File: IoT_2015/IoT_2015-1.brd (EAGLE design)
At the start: 30 x 20 mm, 28 parts, among them Y1 ABLS-16.000MHZ-B4-T

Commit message: FITT EAGLE
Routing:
- net GND: track 144.9 -> 91.2 mm, vias 4 -> 2
- net N$27: track 0.00 -> 2.60 mm
- net N$21: track 0.00 -> 2.55 mm
- net VDD: track 103.9 -> 106.3 mm
- net N$28: track 0.00 -> 2.35 mm
- net N$42: track 0.00 -> 1.95 mm
- net N$44: track 0.00 -> 1.83 mm
- net N$32: track 0.00 -> 1.75 mm
- net N$29: track 0.00 -> 1.55 mm
- net N$19: track 0.00 -> 1.50 mm
- net N$43: track 0.00 -> 1.23 mm
- net N$40: track 0.00 -> 0.85 mm
- net N$38: track 0.00 -> 0.65 mm
- net N$37: track 0.00 -> 0.65 mm
- net N$14: track 0.00 -> 0.60 mm
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
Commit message: Test av jordlager
titta på dennna?
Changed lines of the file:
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@@
 <?xml version="1.0" encoding="utf-8"?>
 <!DOCTYPE eagle SYSTEM "eagle.dtd">
-<eagle version="7.3.0">
+<eagle version="7.2.0">
 <drawing>
 <settings>
@@
 <wire x1="13.96" y1="10.68" x2="16.4" y2="10.68" width="0.254" layer="1"/>
 <wire x1="16.4" y1="10.68" x2="16.4" y2="11.08" width="0.254" layer="1"/>
+<polygon width="0.01" layer="1" spacing="0.05" isolate="0.012">
+<vertex x="0" y="0"/>
+<vertex x="0" y="20"/>
+<vertex x="30" y="20"/>
+<vertex x="30" y="0"/>
+</polygon>
+<wire x1="16.21" y1="15.13" x2="13.35" y2="15.18" width="0" layer="19" extent="1-1"/>
+<wire x1="20.07" y1="12.25" x2="19.49" y2="15.13" width="0" layer="19" extent="1-1"/>
+<wire x1="8.92" y1="15.18" x2="13.2588" y2="15.3162" width="0" layer="19" extent="1-1"/>
 </signal>
 <signal name="N$3">

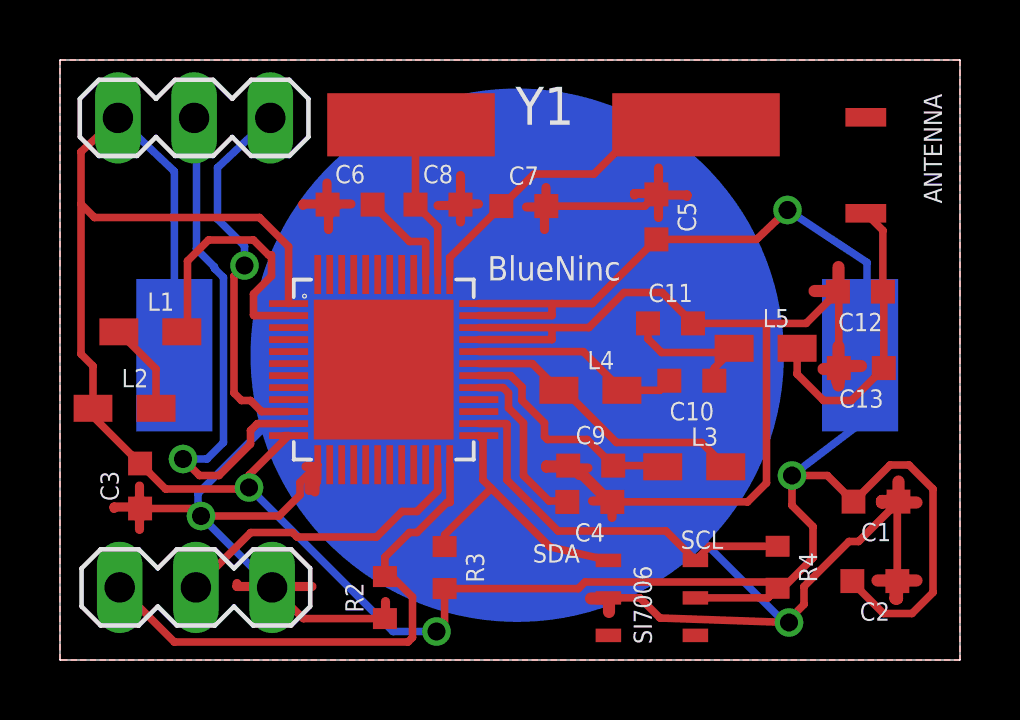
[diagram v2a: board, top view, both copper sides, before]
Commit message: groundplane
groundplane for top and bottom layer are done. To adjust the width of
the copper pour: Set the width of the polygon to draw around the design.
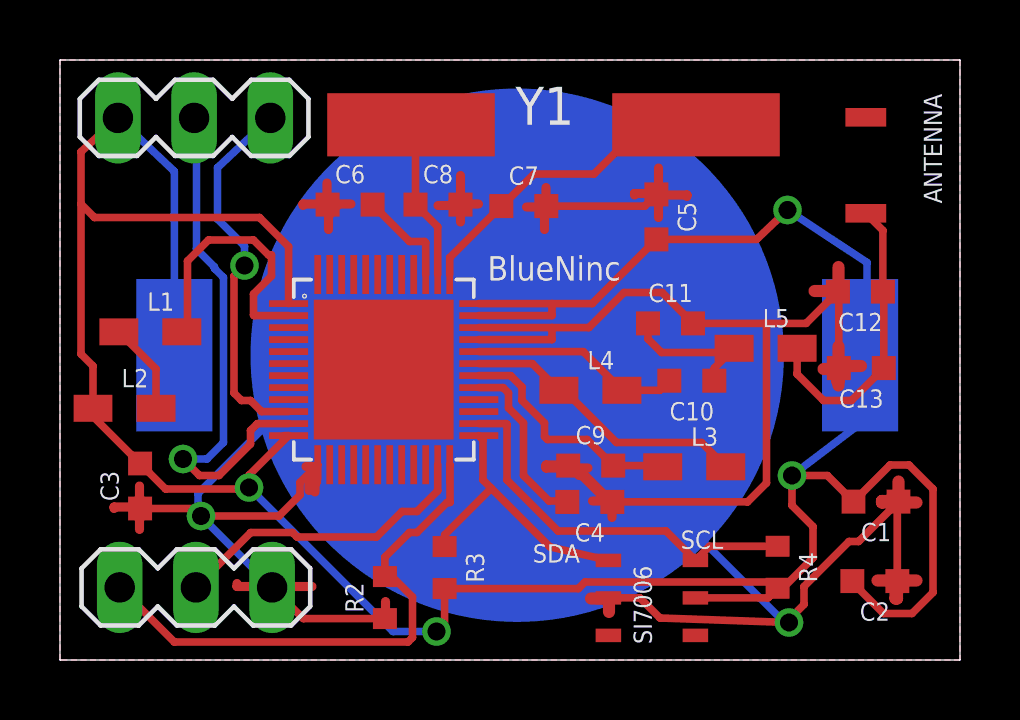
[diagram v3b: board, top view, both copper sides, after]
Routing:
- added copper zone on layer 1, net N$45
- added copper zone on layer 16, net N$46
- removed copper zone on layer 1, net GND

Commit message: Uploaded gerber files
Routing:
- net GND: track 91.2 -> 150.8 mm, vias 2 -> 5
- net N$21: track 2.55 -> 0.00 mm
- net N$28: track 2.35 -> 0.00 mm
- net N$42: track 1.95 -> 0.00 mm
- net N$32: track 1.75 -> 0.00 mm
- net N$29: track 1.55 -> 0.00 mm
- net N$19: track 1.50 -> 0.00 mm
- net N$43: track 1.23 -> 0.00 mm
- net N$40: track 0.85 -> 0.00 mm
- net N$38: track 0.65 -> 0.00 mm
- net N$37: track 0.65 -> 0.00 mm
- net N$14: track 0.60 -> 0.00 mm
- net N$25: track 0.60 -> 0.00 mm
- net N$36: track 0.55 -> 0.00 mm
- net N$30: track 0.55 -> 0.00 mm
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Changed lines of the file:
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@@
 <?xml version="1.0" encoding="utf-8"?>
 <!DOCTYPE eagle SYSTEM "eagle.dtd">
-<eagle version="7.2.0">
+<eagle version="7.3.0">
 <drawing>
 <settings>
@@
 <contactref element="SI7006" pad="GND"/>
 <contactref element="JTAG" pad="3"/>
-<wire x1="13.2588" y1="15.3162" x2="13.35" y2="15.18" width="0.254" layer="1"/>
 <wire x1="27.91" y1="2.63" x2="27.91" y2="5.24" width="0.254" layer="1"/>
 <wire x1="27.91" y1="5.24" x2="27.95" y2="5.28" width="0.254" layer="1"/>
-<wire x1="25.96" y1="9.73" x2="25.96" y2="12.25" width="0.254" layer="1"/>
-<wire x1="25.96" y1="12.25" x2="25.93" y2="12.28" width="0.254" layer="1"/>
 <wire x1="18.28" y1="2.07" x2="19.33" y2="2.07" width="0.254" layer="1"/>
 <wire x1="19.33" y1="2.07" x2="20" y2="1.4" width="0.254" layer="1"/>
@@
 <wire x1="26.3" y1="3.95" x2="26.62" y2="3.95" width="0.254" layer="1"/>
 <wire x1="26.62" y1="3.95" x2="27.95" y2="5.28" width="0.254" layer="1"/>
-<wire x1="16.94" y1="6.48" x2="17.2" y2="6.48" width="0.254" layer="1"/>
-<wire x1="17.2" y1="6.48" x2="18.41" y2="5.27" width="0.254" layer="1"/>
 <wire x1="21.1" y1="11.22" x2="23.5" y2="11.22" width="0.254" layer="1"/>
 <wire x1="23.5" y1="11.22" x2="24.87" y2="11.22" width="0.254" layer="1"/>
@@
 <wire x1="13.96" y1="10.68" x2="16.4" y2="10.68" width="0.254" layer="1"/>
 <wire x1="16.4" y1="10.68" x2="16.4" y2="11.08" width="0.254" layer="1"/>
-<wire x1="13.35" y1="15.18" x2="16.21" y2="15.13" width="0" layer="19" extent="1-1"/>
-<wire x1="20.07" y1="12.25" x2="19.49" y2="15.13" width="0" layer="19" extent="1-1"/>
-<wire x1="15.24" y1="10.16" x2="16.4" y2="10.68" width="0" layer="19" extent="1-16"/>
-<wire x1="8.92" y1="15.18" x2="13.2588" y2="15.3162" width="0" layer="19" extent="1-1"/>
+<wire x1="16.94" y1="6.48" x2="17.2" y2="6.48" width="0.254" layer="1"/>
+<wire x1="17.2" y1="6.48" x2="18.41" y2="5.27" width="0.254" layer="1"/>
+<wire x1="25.96" y1="9.73" x2="25.96" y2="12.25" width="0.254" layer="1"/>
+<wire x1="25.96" y1="12.25" x2="25.93" y2="12.28" width="0.254" layer="1"/>
+<wire x1="19.49" y1="15.13" x2="23.13" y2="15.13" width="0.254" layer="1"/>
+<wire x1="23.13" y1="15.13" x2="24.3" y2="16.3" width="0.254" layer="1"/>
+<wire x1="24.3" y1="16.3" x2="25" y2="16.3" width="0.254" layer="1"/>
+<via x="25" y="16.3" extent="1-16" drill="0.6"/>
+<wire x1="25" y1="16.3" x2="21.38" y2="16.3" width="0.254" layer="16"/>
+<wire x1="21.38" y1="16.3" x2="15.24" y2="10.16" width="0.254" layer="16"/>
+<wire x1="13.35" y1="15.18" x2="13.35" y2="15.25" width="0.254" layer="1"/>
+<wire x1="13.35" y1="15.25" x2="14.3" y2="16.2" width="0.254" layer="1"/>
+<wire x1="14.3" y1="16.2" x2="14.75" y2="16.2" width="0.254" layer="1"/>
+<wire x1="14.75" y1="16.2" x2="17.95" y2="19.4" width="0.254" layer="1"/>
+<wire x1="17.95" y1="19.4" x2="24.25" y2="19.4" width="0.254" layer="1"/>
+<wire x1="24.25" y1="19.4" x2="25.05" y2="18.6" width="0.254" layer="1"/>
+<wire x1="25.05" y1="18.6" x2="25.05" y2="16.35" width="0.254" layer="1"/>
+<wire x1="25.05" y1="16.35" x2="25" y2="16.3" width="0.254" layer="1"/>
+<wire x1="8.92" y1="15.18" x2="7.37" y2="15.18" width="0.254" layer="1"/>
+<wire x1="7.37" y1="15.18" x2="6.85" y2="15.7" width="0.254" layer="1"/>
+<via x="6.85" y="15.7" extent="1-16" drill="0.6"/>
+<wire x1="6.85" y1="15.7" x2="9.7" y2="15.7" width="0.254" layer="16"/>
+<wire x1="9.7" y1="15.7" x2="15.24" y2="10.16" width="0.254" layer="16"/>
+<wire x1="15.24" y1="10.16" x2="21.46" y2="10.16" width="0.254" layer="16"/>
+<wire x1="21.46" y1="10.16" x2="24.55" y2="13.25" width="0.254" layer="16"/>
+<via x="24.55" y="13.25" extent="1-16" drill="0.6"/>
+<wire x1="24.55" y1="13.25" x2="24.96" y2="13.25" width="0.254" layer="1"/>
+<wire x1="24.96" y1="13.25" x2="25.93" y2="12.28" width="0.254" layer="1"/>
 </signal>
 <signal name="N$3">
@@
 </signal>
 <signal name="N$13">
-<wire x1="25.95" y1="12.6" x2="25.95" y2="13.1" width="0.4064" layer="1"/>
 </signal>
 <signal name="N$14">
-<wire x1="25.75" y1="12.3" x2="25.15" y2="12.3" width="0.4064" layer="1"/>
 </signal>
 <signal name="N$15">
-<wire x1="25.45" y1="9.7" x2="25.9" y2="9.7" width="0.4064" layer="1"/>
-<wire x1="25.9" y1="9.7" x2="25.9" y2="9.75" width="0.4064" layer="1"/>
 </signal>
 <signal name="N$16">
-<wire x1="25.9" y1="9.3" x2="25.95" y2="9.3" width="0.4064" layer="1"/>
-<wire x1="25.95" y1="9.3" x2="25.95" y2="9.15" width="0.4064" layer="1"/>
-</signal>
-<signal name="N$17">
-<wire x1="26.35" y1="9.8" x2="26.7" y2="9.8" width="0.4064" layer="1"/>
 </signal>
 <signal name="N$18">
-<wire x1="25.95" y1="10" x2="25.95" y2="10.45" width="0.4064" layer="1"/>
 </signal>
 <signal name="N$19">
-<wire x1="27.7" y1="5.3" x2="27.4" y2="5.3" width="0.4064" layer="1"/>
-<wire x1="27.4" y1="5.3" x2="27.4" y2="5.25" width="0.4064" layer="1"/>
-<wire x1="27.4" y1="5.25" x2="28.55" y2="5.25" width="0.4064" layer="1"/>
 </signal>
 <signal name="N$20">
-<wire x1="27.95" y1="5.95" x2="27.95" y2="5.4" width="0.4064" layer="1"/>
 </signal>
 <signal name="N$21">
-<wire x1="27.85" y1="2.65" x2="27.25" y2="2.65" width="0.4064" layer="1"/>
-<wire x1="27.85" y1="2.65" x2="27.9" y2="2.65" width="0.4064" layer="1"/>
-<wire x1="27.9" y1="2.65" x2="27.9" y2="2.05" width="0.4064" layer="1"/>
-<wire x1="27.9" y1="2.05" x2="27.85" y2="2.05" width="0.4064" layer="1"/>
-<wire x1="27.85" y1="2.05" x2="27.85" y2="2.65" width="0.4064" layer="1"/>
-<wire x1="27.9" y1="2.65" x2="28.55" y2="2.65" width="0.4064" layer="1"/>
 </signal>
 <signal name="N$22">
-<wire x1="18.3" y1="1.9" x2="18.3" y2="1.6" width="0.4064" layer="1"/>
 </signal>
 <signal name="N$23">
-<wire x1="18.25" y1="2.05" x2="17.7" y2="2.05" width="0.4064" layer="1"/>
 </signal>
 <signal name="N$24">
 <wire x1="18.35" y1="5.05" x2="18.4" y2="5.05" width="0.3048" layer="1"/>
-<wire x1="18.4" y1="5.05" x2="18.4" y2="4.75" width="0.3048" layer="1"/>
 </signal>
 <signal name="N$25">
-<wire x1="17.75" y1="5.3" x2="18.3" y2="5.3" width="0.3048" layer="1"/>
-<wire x1="18.3" y1="5.3" x2="18.3" y2="5.35" width="0.3048" layer="1"/>
 </signal>
 <signal name="N$26">
-<wire x1="10.85" y1="1.95" x2="10.85" y2="1.6" width="0.3048" layer="1"/>
 </signal>
 <signal name="N$27">
@@
 </signal>
 <signal name="N$28">
-<wire x1="2.65" y1="4.35" x2="2.65" y2="5.1" width="0.3048" layer="1"/>
-<wire x1="2.65" y1="5.1" x2="2.65" y2="5.8" width="0.3048" layer="1"/>
-<wire x1="2.65" y1="5.1" x2="1.8" y2="5.1" width="0.3048" layer="1"/>
-<wire x1="1.8" y1="5.1" x2="1.8" y2="5.05" width="0.3048" layer="1"/>
-</signal>
-<signal name="N$29">
-<wire x1="8.9" y1="15.9" x2="8.9" y2="15.25" width="0.3048" layer="1"/>
-<wire x1="8.9" y1="15.25" x2="8.85" y2="15.25" width="0.3048" layer="1"/>
-<wire x1="8.85" y1="15.25" x2="8.85" y2="15.2" width="0.3048" layer="1"/>
-<wire x1="8.85" y1="15.2" x2="8.1" y2="15.2" width="0.3048" layer="1"/>
-<wire x1="8.1" y1="15.2" x2="8.1" y2="15.15" width="0.3048" layer="1"/>
 </signal>
 <signal name="N$30">
-<wire x1="9" y1="14.85" x2="8.95" y2="14.85" width="0.3048" layer="1"/>
-<wire x1="8.95" y1="14.85" x2="8.95" y2="14.35" width="0.3048" layer="1"/>
 </signal>
 <signal name="N$31">
-<wire x1="9.7" y1="15.2" x2="9.25" y2="15.2" width="0.3048" layer="1"/>
-<wire x1="9.25" y1="15.2" x2="9.25" y2="15.15" width="0.3048" layer="1"/>
 </signal>
 <signal name="N$32">
-<wire x1="12.6" y1="15.15" x2="13.05" y2="15.15" width="0.3048" layer="1"/>
-<wire x1="13.05" y1="15.15" x2="13.05" y2="15.2" width="0.3048" layer="1"/>
-<wire x1="13.05" y1="15.2" x2="13.35" y2="15.2" width="0.3048" layer="1"/>
-<wire x1="13.35" y1="15.2" x2="13.35" y2="16.15" width="0.3048" layer="1"/>
 </signal>
 <signal name="N$33">
-<wire x1="13.6" y1="15.2" x2="13.95" y2="15.2" width="0.3048" layer="1"/>
 </signal>
 <signal name="N$34">
-<wire x1="13.35" y1="14.6" x2="13.35" y2="15.1" width="0.3048" layer="1"/>
 </signal>
 <signal name="N$35">
-<wire x1="15.55" y1="15.1" x2="15.95" y2="15.1" width="0.3048" layer="1"/>
-<wire x1="15.95" y1="15.1" x2="15.95" y2="15.05" width="0.3048" layer="1"/>
 </signal>
 <signal name="N$36">
-<wire x1="16.3" y1="15.3" x2="16.2" y2="15.3" width="0.3048" layer="1"/>
-<wire x1="16.2" y1="15.3" x2="16.2" y2="15.75" width="0.3048" layer="1"/>
 </signal>
 <signal name="N$37">
-<wire x1="16.2" y1="14.95" x2="16.15" y2="14.95" width="0.3048" layer="1"/>
-<wire x1="16.15" y1="14.95" x2="16.15" y2="14.35" width="0.3048" layer="1"/>
 </signal>
 <signal name="N$38">
-<wire x1="19.75" y1="15.55" x2="19.15" y2="15.55" width="0.3048" layer="1"/>
-<wire x1="19.15" y1="15.55" x2="19.15" y2="15.5" width="0.3048" layer="1"/>
 </signal>
 <signal name="N$39">
-<wire x1="19.95" y1="15.85" x2="19.95" y2="16.4" width="0.3048" layer="1"/>
 </signal>
 <signal name="N$40">
-<wire x1="20.1" y1="15.5" x2="20.9" y2="15.5" width="0.3048" layer="1"/>
-<wire x1="20.9" y1="15.5" x2="20.9" y2="15.45" width="0.3048" layer="1"/>
 </signal>
 <signal name="N$41">
-<wire x1="19.95" y1="14.75" x2="19.95" y2="15.2" width="0.3048" layer="1"/>
 </signal>
 <signal name="N$42">
-<wire x1="16.65" y1="6.5" x2="16.2" y2="6.5" width="0.3048" layer="1"/>
-<wire x1="16.2" y1="6.5" x2="16.2" y2="6.4" width="0.3048" layer="1"/>
-<wire x1="16.2" y1="6.4" x2="17.6" y2="6.4" width="0.3048" layer="1"/>
 </signal>
 <signal name="N$43">
-<wire x1="17.3" y1="6.15" x2="17.4" y2="6.15" width="0.3048" layer="1"/>
-<wire x1="17.4" y1="6.15" x2="18.2" y2="5.35" width="0.3048" layer="1"/>
 </signal>
 <signal name="N$44">

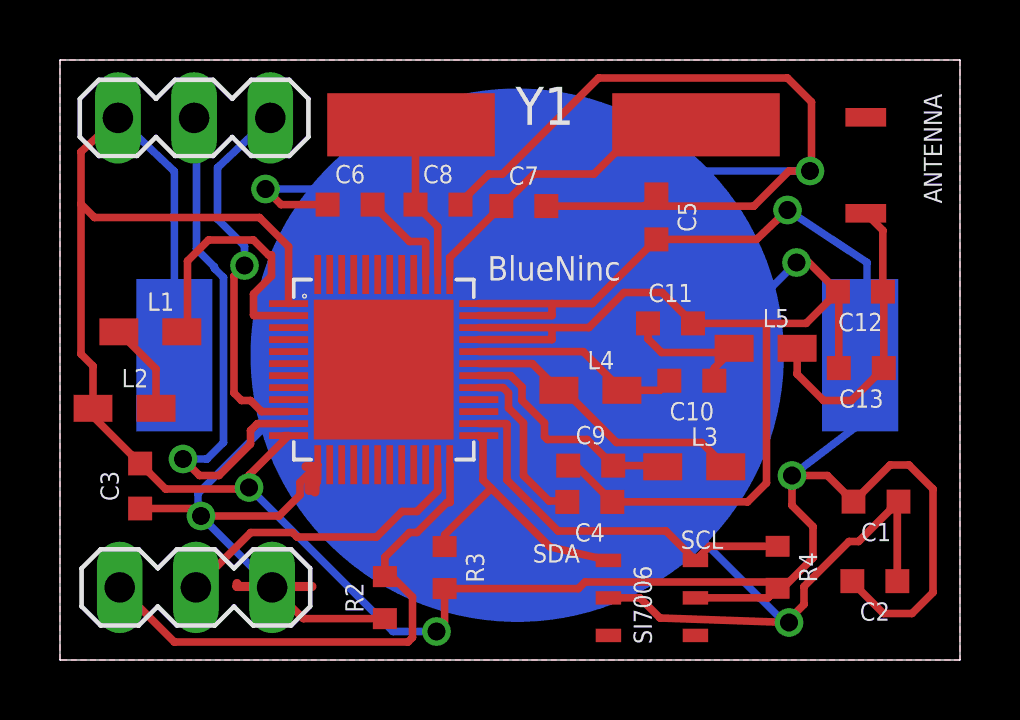
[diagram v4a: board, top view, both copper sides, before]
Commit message: Generated gerberfile
Autoroute and generate ground pour layer were carried out. Check the
gerberfile.
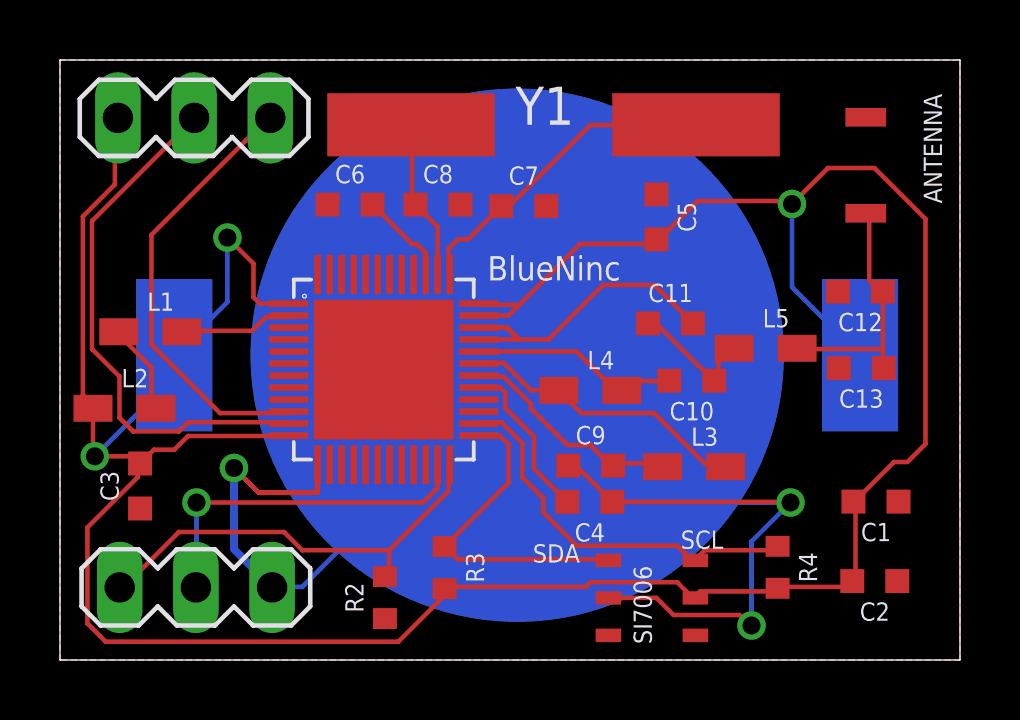
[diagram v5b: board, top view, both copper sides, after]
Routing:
- net GND: track 150.8 -> 58.9 mm, vias 5 -> 3
- net N$2: track 9.16 -> 3.81 mm
- net N$29: track 0.00 -> 4.10 mm
- net SWDCLK: track 18.0 -> 14.6 mm
- net P0.06: track 12.5 -> 14.8 mm, vias 1 -> 0
- net VDD: track 106.3 -> 104.0 mm, vias 4 -> 3
- net SDA: track 9.28 -> 11.4 mm
- net N$44: track 1.83 -> 0.00 mm
- net N$4: track 9.97 -> 8.31 mm
- net SWDIO/NRESET: track 10.4 -> 11.9 mm, vias 0 -> 1
- net N$27: track 2.60 -> 1.42 mm
- net N$11: track 4.99 -> 4.39 mm
- net P0.07: track 17.5 -> 17.8 mm, vias 1 -> 0
- added copper zone on layer 1, net GND
- added copper zone on layer 16, net N$17
- removed copper zone on layer 1, net N$45
- removed copper zone on layer 16, net N$46
